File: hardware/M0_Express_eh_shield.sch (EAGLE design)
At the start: 30 parts, among them U1 TLV3691, U2 AB0815, U3 Value, U4 MIC841, U5 TPS781, X2 ABS05-32.768KHZ-9-T

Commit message: updates and programmer
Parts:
- removed JP11: (no value), SparkFun-Connectors:M06
- added JP2: (no value), SparkFun-Connectors:M05X21.27MM
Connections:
- net GND: now also JP2.10, JP2.9; no longer JP11.1
- net MSP430_RST: now also JP2.5, JP2.6; no longer JP11.3
- net MSP430_TEST: now also JP2.3, JP2.4; no longer JP11.2
- net RX_DEBUG: now also JP2.2; no longer JP11.4
- net TX_DEBUG: now also JP2.7, JP2.8; no longer JP11.5
- net VCC: now also JP2.1; no longer JP11.6
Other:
- note added: "Debug"
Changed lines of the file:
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@@
 </variantdefs>
 <classes>
-<class number="0" name="default" width="0" drill="0">
+<class number="0" name="default" width="0.3302" drill="0.3302">
+<clearance class="0" value="0.1524"/>
 </class>
 <class number="1" name="USB" width="0" drill="0">
@@
 <part name="GND30" library="SparkFun-Aesthetics" deviceset="GND" device=""/>
 <part name="SUPPLY2" library="SparkFun-Aesthetics" deviceset="VCC" device=""/>
-<part name="JP11" library="SparkFun-Connectors" deviceset="M06" device="">
-<attribute name="DIGIKEY" value="S9010E-06-ND"/>
-<attribute name="MPN" value="LPPB061NGCN-RC"/>
-</part>
-<part name="GND21" library="SparkFun-Aesthetics" deviceset="GND" device=""/>
-<part name="SUPPLY3" library="SparkFun-Aesthetics" deviceset="VCC" device=""/>
 <part name="GND10" library="SparkFun-Aesthetics" deviceset="GND" device=""/>
 <part name="SUPPLY4" library="SparkFun-Aesthetics" deviceset="VCC" device=""/>
@@
 <part name="SUPPLY8" library="SparkFun-Aesthetics" deviceset="VCC" device=""/>
 <part name="D3" library="SparkFun-Sensors" deviceset="SOLAR-IXYS" device="-">
-<attribute name="DIGIKEY" value="KXOB25-02X8F-ND	"/>
+<attribute name="DIGIKEY" value="KXOB25-02X8F-ND "/>
 </part>
 <part name="D4" library="SparkFun-Sensors" deviceset="SOLAR-IXYS" device="-">
-<attribute name="DIGIKEY" value="KXOB25-02X8F-ND	"/>
+<attribute name="DIGIKEY" value="KXOB25-02X8F-ND "/>
 </part>
 <part name="GND11" library="SparkFun-Aesthetics" deviceset="GND" device=""/>
 <part name="JP3" library="SparkFun-Connectors" deviceset="M02" device="LOCK"/>
+<part name="JP2" library="SparkFun-Connectors" deviceset="M05X2" device="1.27MM">
+<attribute name="DIGIKEY" value="1175-1627-ND "/>
+</part>
+<part name="SUPPLY3" library="SparkFun-Aesthetics" deviceset="VCC" device=""/>
+<part name="GND15" library="SparkFun-Aesthetics" deviceset="GND" device=""/>
+<part name="GND16" library="SparkFun-Aesthetics" deviceset="GND" device=""/>
 </parts>
 <sheets>
@@
 <text x="312.166" y="110.236" size="1.778" layer="97">To M0</text>
 <text x="96.52" y="229.87" size="2.54" layer="91" ratio="12">Connect Solar</text>
+<text x="58.42" y="154.94" size="2.54" layer="94" ratio="15" align="center">Debug</text>
 </plain>
 <instances>
@@
 <instance part="GND30" gate="1" x="66.04" y="27.94"/>
 <instance part="SUPPLY2" gate="G$1" x="251.46" y="81.28"/>
-<instance part="JP11" gate="G$1" x="22.86" y="139.7">
-<attribute name="MPN" x="22.86" y="139.7" size="1.27" layer="96" display="off"/>
-<attribute name="DIGIKEY" x="22.86" y="139.7" size="1.27" layer="96" display="off"/>
-</instance>
-<instance part="GND21" gate="1" x="30.48" y="129.54"/>
-<instance part="SUPPLY3" gate="G$1" x="30.48" y="149.86"/>
 <instance part="GND10" gate="1" x="223.52" y="17.78"/>
 <instance part="SUPPLY4" gate="G$1" x="99.06" y="157.48"/>
@@
 <attribute name="NAME" x="96.52" y="218.186" size="1.778" layer="95"/>
 </instance>
+<instance part="JP2" gate="G$1" x="55.88" y="139.7">
+<attribute name="DIGIKEY" x="55.88" y="139.7" size="1.27" layer="96" display="off"/>
+</instance>
+<instance part="SUPPLY3" gate="G$1" x="45.72" y="147.32"/>
+<instance part="GND15" gate="1" x="45.72" y="129.54"/>
+<instance part="GND16" gate="1" x="66.04" y="129.54"/>
 </instances>
 <busses>
@@
 <junction x="66.04" y="33.02"/>
 <pinref part="GND30" gate="1" pin="GND"/>
-</segment>
-<segment>
-<pinref part="JP11" gate="G$1" pin="1"/>
-<wire x1="27.94" y1="134.62" x2="30.48" y2="134.62" width="0.1524" layer="91"/>
-<wire x1="30.48" y1="134.62" x2="30.48" y2="132.08" width="0.1524" layer="91"/>
-<pinref part="GND21" gate="1" pin="GND"/>
 </segment>
 <segment>
@@
 <pinref part="GND11" gate="1" pin="GND"/>
 </segment>
+<segment>
+<pinref part="JP2" gate="G$1" pin="9"/>
+<wire x1="48.26" y1="134.62" x2="45.72" y2="134.62" width="0.1524" layer="91"/>
+<wire x1="45.72" y1="134.62" x2="45.72" y2="132.08" width="0.1524" layer="91"/>
+<pinref part="GND15" gate="1" pin="GND"/>
+</segment>
+<segment>
+<pinref part="JP2" gate="G$1" pin="10"/>
+<wire x1="63.5" y1="134.62" x2="66.04" y2="134.62" width="0.1524" layer="91"/>
+<wire x1="66.04" y1="134.62" x2="66.04" y2="132.08" width="0.1524" layer="91"/>
+<pinref part="GND16" gate="1" pin="GND"/>
+</segment>
 </net>
 <net name="AREF" class="4">
@@
 </segment>
 <segment>
-<pinref part="JP11" gate="G$1" pin="6"/>
-<wire x1="27.94" y1="147.32" x2="30.48" y2="147.32" width="0.1524" layer="91"/>
-<wire x1="30.48" y1="147.32" x2="30.48" y2="149.86" width="0.1524" layer="91"/>
-<pinref part="SUPPLY3" gate="G$1" pin="VCC"/>
-</segment>
-<segment>
 <pinref part="U3" gate="A" pin="DVCC3"/>
 <wire x1="101.6" y1="139.7" x2="99.06" y2="139.7" width="0.1524" layer="91"/>
@@
 <pinref part="SUPPLY8" gate="G$1" pin="VCC"/>
 </segment>
+<segment>
+<pinref part="JP2" gate="G$1" pin="1"/>
+<wire x1="48.26" y1="144.78" x2="45.72" y2="144.78" width="0.1524" layer="91"/>
+<wire x1="45.72" y1="144.78" x2="45.72" y2="147.32" width="0.1524" layer="91"/>
+<pinref part="SUPPLY3" gate="G$1" pin="VCC"/>
+</segment>
 </net>
 <net name="REG_SET" class="0">
@@
 <net name="MSP430_TEST" class="0">
 <segment>
-<pinref part="JP11" gate="G$1" pin="2"/>
-<wire x1="27.94" y1="137.16" x2="30.48" y2="137.16" width="0.1524" layer="91"/>
-<label x="30.48" y="137.16" size="1.27" layer="95" xref="yes"/>
-</segment>
-<segment>
 <pinref part="U3" gate="A" pin="TEST_SBWTCK"/>
 <wire x1="220.98" y1="68.58" x2="226.06" y2="68.58" width="0.1524" layer="91"/>
 <label x="226.06" y="68.58" size="1.778" layer="95" xref="yes"/>
+</segment>
+<segment>
+<pinref part="JP2" gate="G$1" pin="3"/>
+<wire x1="48.26" y1="142.24" x2="45.72" y2="142.24" width="0.1524" layer="91"/>
+<label x="45.72" y="142.24" size="1.27" layer="95" rot="R180" xref="yes"/>
+</segment>
+<segment>
+<pinref part="JP2" gate="G$1" pin="4"/>
+<wire x1="63.5" y1="142.24" x2="66.04" y2="142.24" width="0.1524" layer="91"/>
+<label x="66.04" y="142.24" size="1.27" layer="95" xref="yes"/>
 </segment>
 </net>
@@
 </segment>
 <segment>
-<pinref part="JP11" gate="G$1" pin="3"/>
-<wire x1="27.94" y1="139.7" x2="30.48" y2="139.7" width="0.1524" layer="91"/>
-<label x="30.48" y="139.7" size="1.27" layer="95" xref="yes"/>
+<pinref part="JP2" gate="G$1" pin="5"/>
+<wire x1="48.26" y1="139.7" x2="45.72" y2="139.7" width="0.1524" layer="91"/>
+<label x="45.72" y="139.7" size="1.27" layer="95" rot="R180" xref="yes"/>
+</segment>
+<segment>
+<pinref part="JP2" gate="G$1" pin="6"/>
+<wire x1="63.5" y1="139.7" x2="66.04" y2="139.7" width="0.1524" layer="91"/>
+<label x="66.04" y="139.7" size="1.27" layer="95" xref="yes"/>
 </segment>
 </net>
@@
 <net name="TX_DEBUG" class="0">
 <segment>
-<pinref part="JP11" gate="G$1" pin="5"/>
-<wire x1="27.94" y1="144.78" x2="30.48" y2="144.78" width="0.1524" layer="91"/>
-<label x="30.48" y="144.78" size="1.27" layer="95" xref="yes"/>
-</segment>
-<segment>
 <pinref part="U3" gate="A" pin="P2.0_TB0.6_UCA0TXD_UCA0SIMO_TB0CLK_ACLK"/>
 <wire x1="220.98" y1="154.94" x2="223.52" y2="154.94" width="0.1524" layer="91"/>
 <label x="223.52" y="154.94" size="1.27" layer="95" xref="yes"/>
 </segment>
+<segment>
+<pinref part="JP2" gate="G$1" pin="7"/>
+<wire x1="45.72" y1="137.16" x2="48.26" y2="137.16" width="0.1524" layer="91"/>
+<label x="45.72" y="137.16" size="1.27" layer="95" rot="R180" xref="yes"/>
+</segment>
+<segment>
+<pinref part="JP2" gate="G$1" pin="8"/>
+<wire x1="63.5" y1="137.16" x2="66.04" y2="137.16" width="0.1524" layer="91"/>
+<label x="66.04" y="137.16" size="1.27" layer="95" xref="yes"/>
+</segment>
 </net>
 <net name="RX_DEBUG" class="0">
-<segment>
-<pinref part="JP11" gate="G$1" pin="4"/>
-<wire x1="27.94" y1="142.24" x2="30.48" y2="142.24" width="0.1524" layer="91"/>
-<label x="30.48" y="142.24" size="1.27" layer="95" xref="yes"/>
-</segment>
 <segment>
 <pinref part="U3" gate="A" pin="P2.1_TB0.0_UCA0RXD_UCA0SOMI"/>
@@
 <label x="223.52" y="152.4" size="1.27" layer="95" xref="yes"/>
 </segment>
-</net>
+<segment>
+<pinref part="JP2" gate="G$1" pin="2"/>
+<wire x1="63.5" y1="144.78" x2="66.04" y2="144.78" width="0.1524" layer="91"/>
+<label x="66.04" y="144.78" size="1.27" layer="95" xref="yes"/>
+</segment>
+</net>

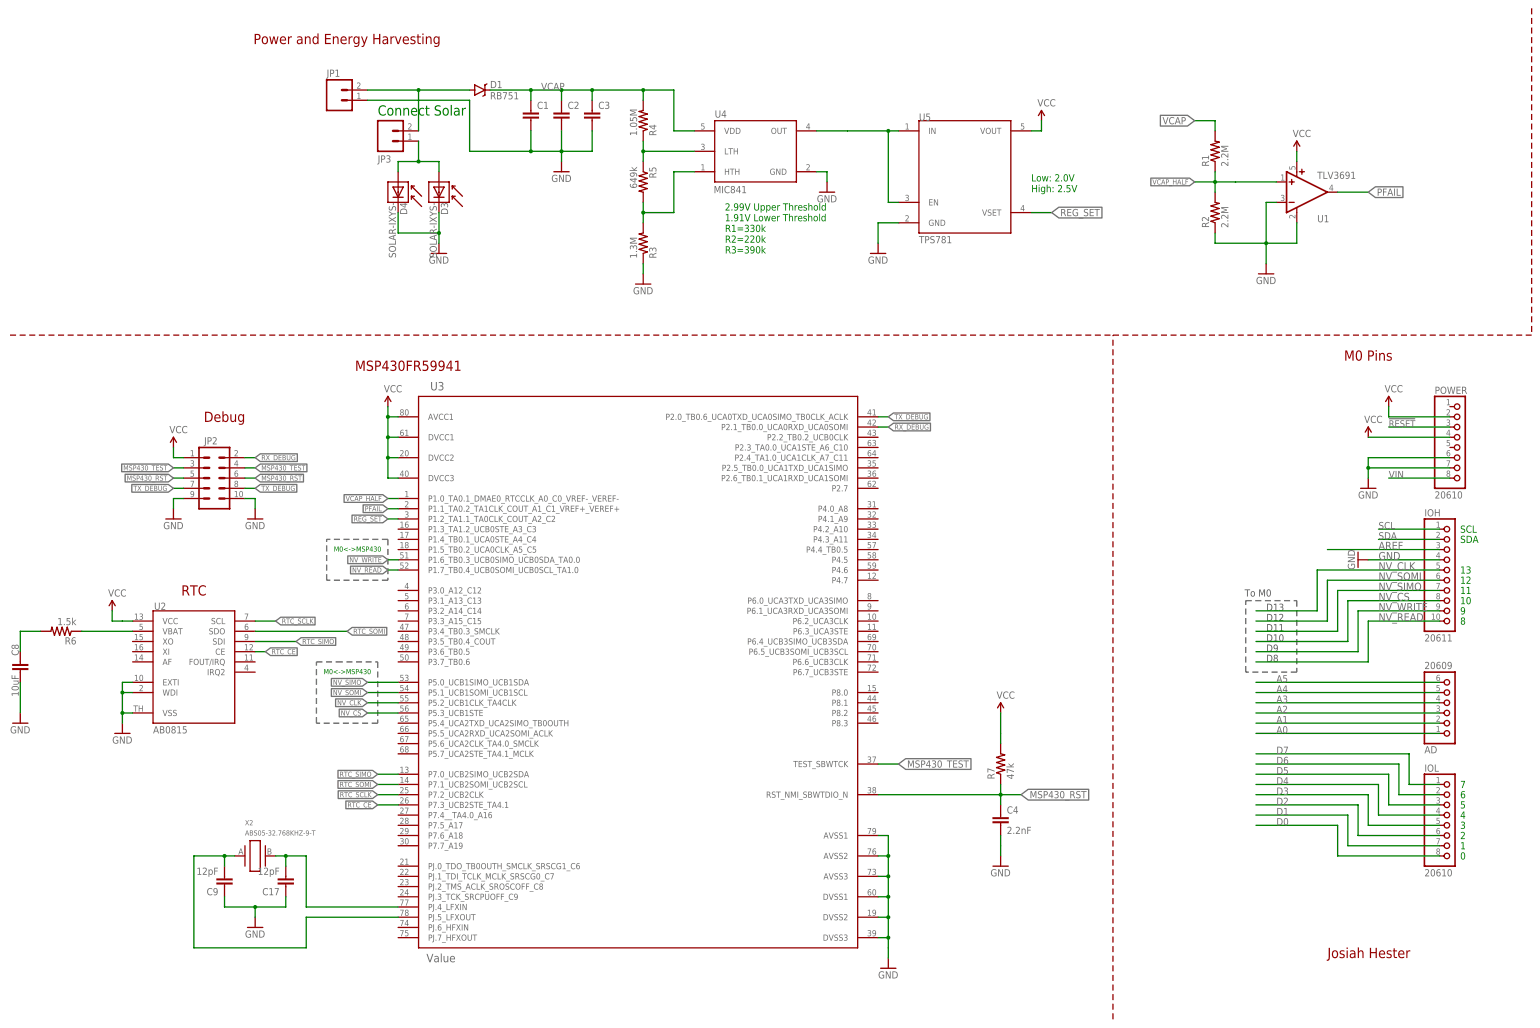
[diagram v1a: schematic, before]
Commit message: finished schematic, basic board layout, need to route and order
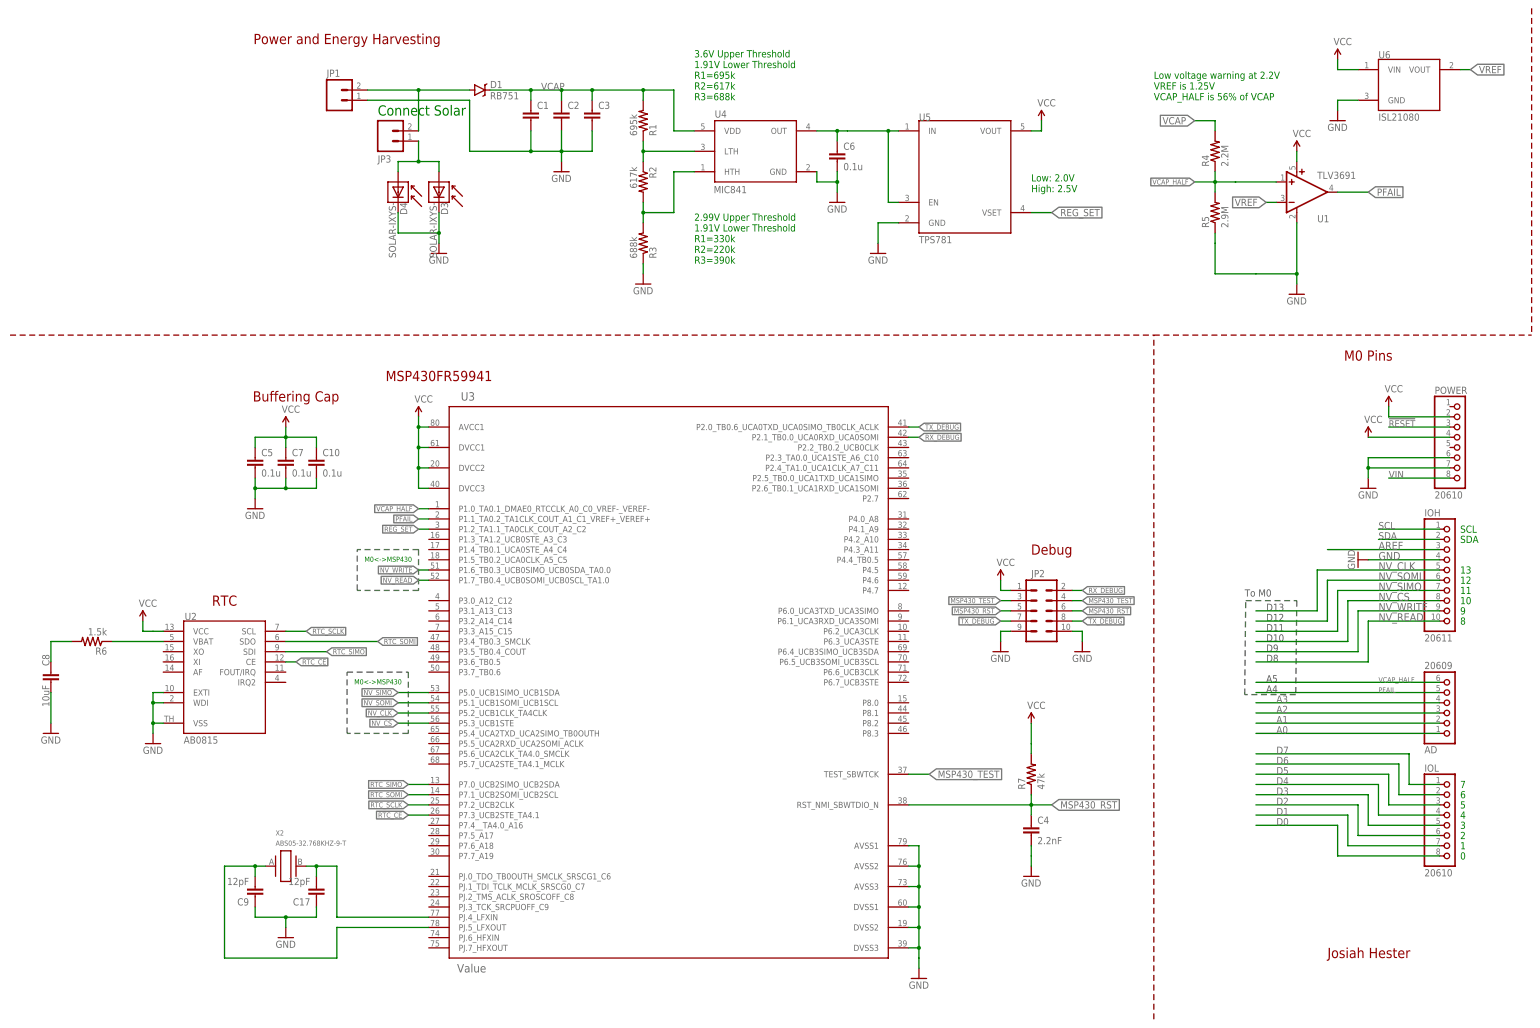
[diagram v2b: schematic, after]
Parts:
- added C10, C5, C6, C7: 0.1u, tiny_passives:C-EU0603
- added U6: ISL21080, isl21080:ISL21080
- R1: value 2.2M -> 695k; DIGIKEY (none) -> 311-316KHRCT-ND; MANUFACTURERPARTNUMBER (none) -> RC0603FR-07316KL; MPN (none) -> RC0603FR-07316KL
- R2: value 2.2M -> 617k; DIGIKEY (none) -> 311-191KHRCT-ND; MANUFACTURERPARTNUMBER (none) -> RC0603FR-07191KL; MPN (none) -> RC0603FR-07191KL
- R3: value 1.3M -> 688k
- R4: value 1.05M -> 2.2M; DIGIKEY 311-316KHRCT-ND -> (none); MANUFACTURERPARTNUMBER RC0603FR-07316KL -> (none); MPN RC0603FR-07316KL -> (none)
- R5: value 649k -> 2.9M; DIGIKEY 311-191KHRCT-ND -> (none); MANUFACTURERPARTNUMBER RC0603FR-07191KL -> (none); MPN RC0603FR-07191KL -> (none)
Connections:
- removed net A4: AD.5
- removed net A5: AD.6
- new net VREF: U1.-IN, U6.VOUT
- net GND: now also C10.2, C5.2, C6.2, C7.2, R5.1, U6.GND; no longer R2.1, U1.-IN
- net N$2: now also R1.1, R2.1; no longer R4.1, R5.1
- net N$3: now also R2.2; no longer R5.2
- net N$7: now also C6.1
- net PFAIL: now also AD.5
- net VCAP_HALF: now also AD.6, R4.1, R5.2; no longer R1.1, R2.2
- net VCC: now also C10.1, C5.1, C7.1, U6.VIN
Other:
- note added: "3.6V Upper Threshold 1.91V Lower Threshold R1=695k R2=617k R3=688k"
- note added: "A4"
- note added: "A5"
- note added: "Buffering Cap"
- note added: "Low voltage warning at 2.2V VREF is 1.25V VCAP_HALF is 56% of VCAP"
- moved on the sheet: C17, C4, C8, C9, JP2, R1, R2, R4, R5, R6, R7, U2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

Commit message: finished hardware
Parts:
- removed C1, C3: (no value), SparkFun-Capacitors:CAP0805
- added C11: 0.1u, tiny_passives:C-EU0603
- added JP4: (no value), SparkFun-Connectors:M025MM
- C2: value (none) -> 10u
- D1: value RB751 -> BAT20JFILM; device SparkFun-DiscreteSemi:DIODE-SCHOTTKY-RB751 -> SparkFun-DiscreteSemi:BAT20JFILM
- U6: DIGIKEY ISL21080DIH312Z-TKTR-ND -> ISL21080DIH312Z-TKTR-ND; MPN ISL21080DIH312Z-TK -> (none)
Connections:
- removed net D6: IOL.2
- removed net D7: IOL.1
- net GND: now also C11.2, JP4.2; no longer C1.2, C3.2
- net NV_READ: now also IOL.1, U3.P1.6_TB0.3_UCB0SIMO_UCB0SDA_TA0.0; no longer IOH.10, U3.P1.7_TB0.4_UCB0SOMI_UCB0SCL_TA1.0
- net NV_WRITE: now also U3.P1.7_TB0.4_UCB0SOMI_UCB0SCL_TA1.0; no longer U3.P1.6_TB0.3_UCB0SIMO_UCB0SDA_TA0.0
- net PFAIL: now also IOL.2, U3.P2.0_TB0.6_UCA0TXD_UCA0SIMO_TB0CLK_ACLK; no longer AD.5, U3.P1.1_TA0.2_TA1CLK_COUT_A1_C1_VREF+_VEREF+
- net REG_SET: now also U3.P3.7_TB0.6; no longer U3.P1.2_TA1.1_TA0CLK_COUT_A2_C2
- net RTC_CE: now also U3.P3.3_A15_C15; no longer U3.P7.3_UCB2STE_TA4.1
- net RTC_SCLK: now also U3.P6.2_UCA3CLK; no longer U3.P7.2_UCB2CLK
- net RTC_SIMO: now also U3.P6.0_UCA3TXD_UCA3SIMO; no longer U3.P7.0_UCB2SIMO_UCB2SDA
- net RTC_SOMI: now also U3.P6.1_UCA3RXD_UCA3SOMI; no longer U3.P7.1_UCB2SOMI_UCB2SCL
- net RX_DEBUG: now also U3.P2.6_TB0.1_UCA1RXD_UCA1SOMI; no longer U3.P2.1_TB0.0_UCA0RXD_UCA0SOMI
- net TX_DEBUG: now also U3.P2.5_TB0.0_UCA1TXD_UCA1SIMO; no longer U3.P2.0_TB0.6_UCA0TXD_UCA0SIMO_TB0CLK_ACLK
- net VCAP: now also JP4.1; no longer C1.1, C3.1
- net VCAP_HALF: now also IOH.10, U3.P7.4__TA4.0_A16; no longer AD.6, U3.P1.0_TA0.1_DMAE0_RTCCLK_A0_C0_VREF-_VEREF-
- net VCC: now also C11.1
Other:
- note added: "D6"
- note added: "D7"
- note added: "SuperCap: FYL0H223ZF"
- moved on the sheet: C2, JP2
